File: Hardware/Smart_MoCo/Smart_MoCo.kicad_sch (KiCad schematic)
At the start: 57 parts, among them J1 Conn_02x02_Counter_Clockwise, Q1 BSS138, Q2 BSS138, Q3 BSS138, U1 VNH5019A-E, U2 STM32F042F6Px, U3 ATA6561, U4 AP62200WU, U5 AP62200WU

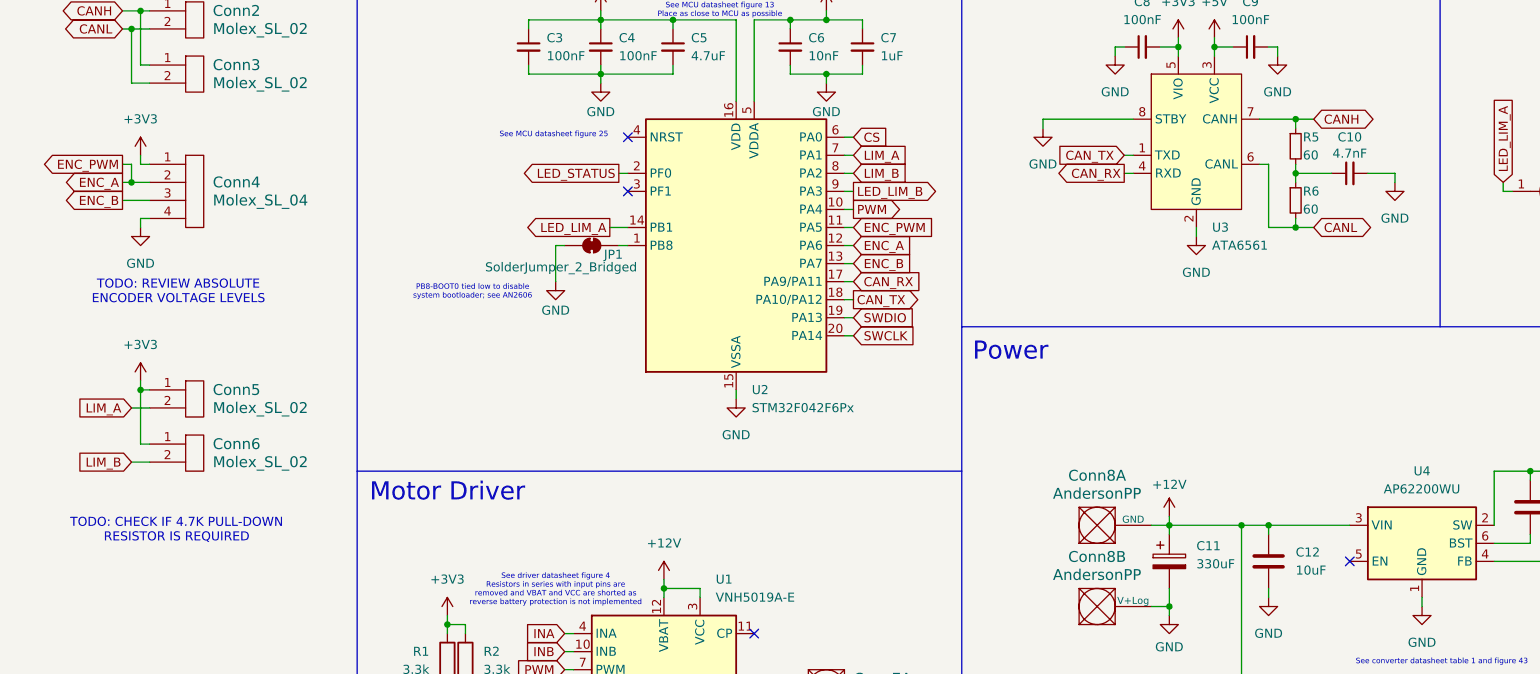
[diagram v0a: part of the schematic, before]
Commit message: Modify CAN circuit
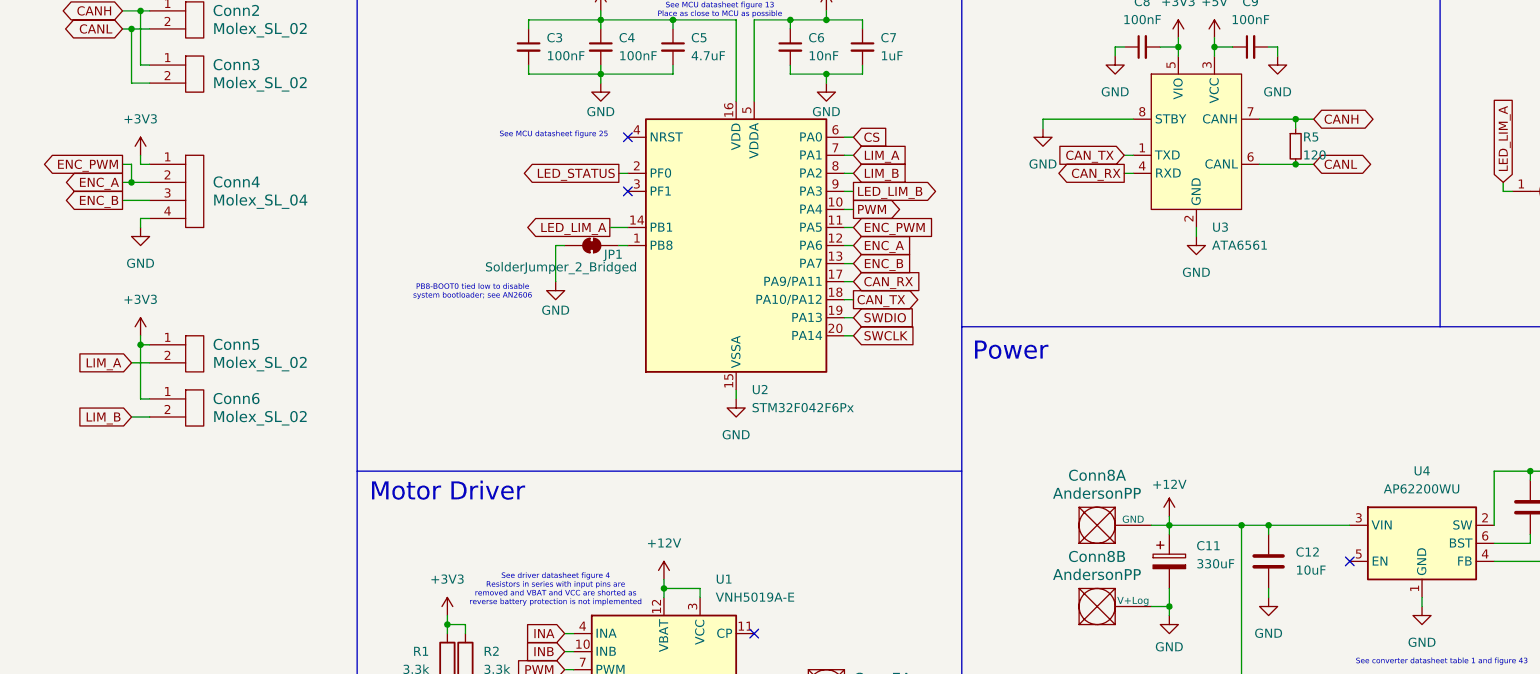
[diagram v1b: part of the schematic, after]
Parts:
- removed C10: 4.7nF, Capacitor_SMD:C_0603_1608Metric_Pad1.08x0.95mm_HandSolder, symbol Device:C_Small
- removed R6: 60, Resistor_SMD:R_0603_1608Metric_Pad0.98x0.95mm_HandSolder, symbol Device:R_Small
- R5: value 60 -> 120
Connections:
- net CANL: now also R5.2
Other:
- note removed: "TODO: CHECK IF 4.7K PULL-DOWN RESISTOR IS REQUIRED"
- note removed: "TODO: REVIEW ABSOLUTE ENCODER VOLTAGE LEVELS"
- moved on the sheet: Conn5, Conn6

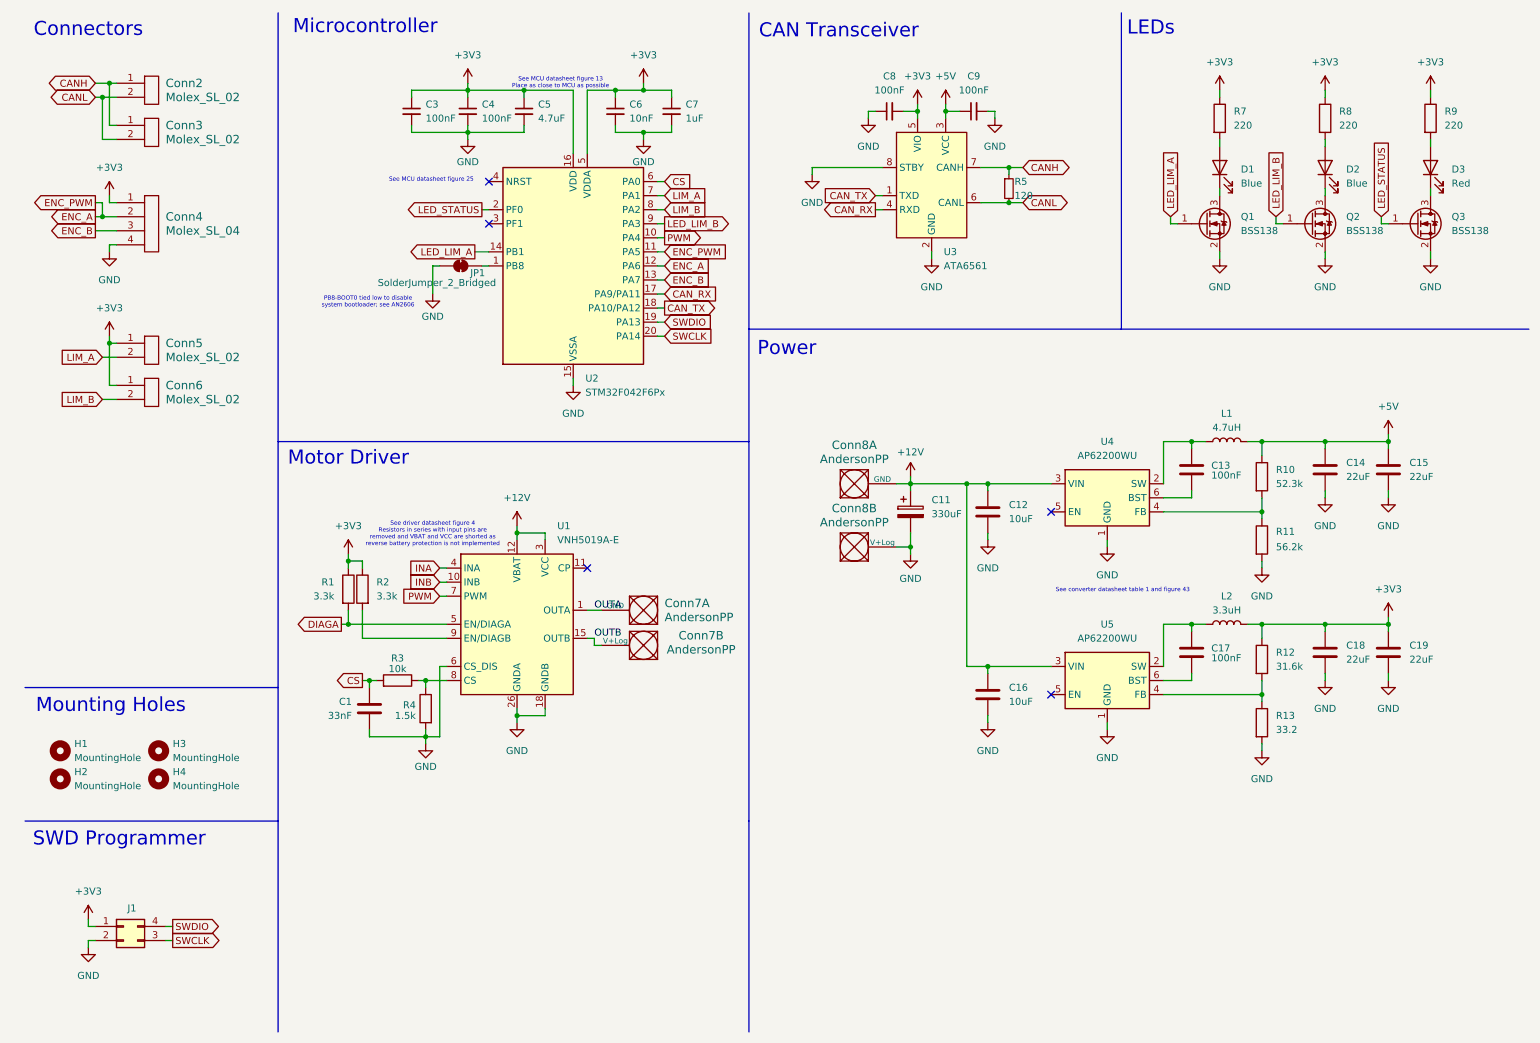
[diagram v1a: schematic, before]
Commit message: Implement schematic first review feedback and finish PCB layout
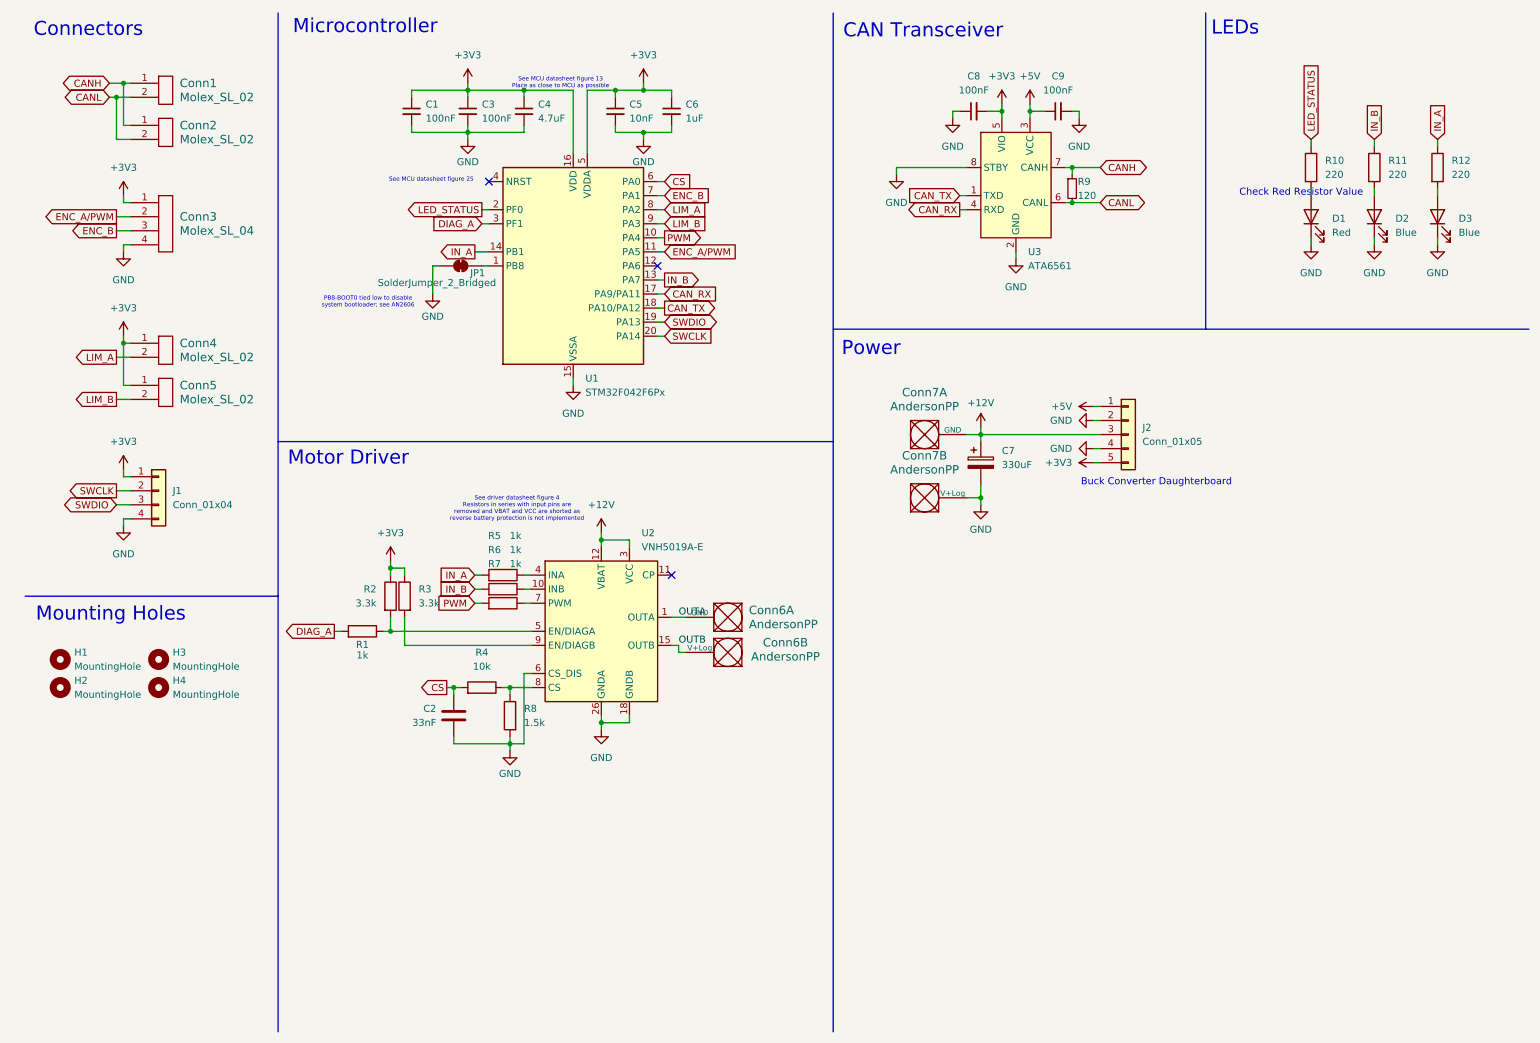
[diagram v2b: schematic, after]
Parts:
- removed C12, C16: 10uF, Capacitor_SMD:C_0603_1608Metric_Pad1.08x0.95mm_HandSolder, symbol Device:C
- removed C13, C17: 100nF, Capacitor_SMD:C_0603_1608Metric_Pad1.08x0.95mm_HandSolder, symbol Device:C
- removed C14, C15, C18, C19: 22uF, Capacitor_SMD:C_0603_1608Metric_Pad1.08x0.95mm_HandSolder, symbol Device:C
- removed J1: Conn_02x02_Counter_Clockwise, Connector_PinHeader_2.54mm:PinHeader_2x02_P2.54mm_Vertical, symbol Connector_Generic:Conn_02x02_Counter_Clockwise
- removed L1: 4.7uH, Inductor_SMD:L_1008_2520Metric_Pad1.43x2.20mm_HandSolder, symbol Device:L
- removed L2: 3.3uH, Inductor_SMD:L_1008_2520Metric_Pad1.43x2.20mm_HandSolder, symbol Device:L
- removed Q1, Q2, Q3: BSS138, Package_TO_SOT_SMD:SOT-23, symbol Transistor_FET:BSS138
- removed R12: 31.6k, Resistor_SMD:R_0603_1608Metric_Pad0.98x0.95mm_HandSolder, symbol Device:R
- removed R13: 33.2, Resistor_SMD:R_0603_1608Metric_Pad0.98x0.95mm_HandSolder, symbol Device:R
- removed R8: 220, Resistor_SMD:R_0603_1608Metric_Pad0.98x0.95mm_HandSolder, symbol Device:R
- removed U4, U5: AP62200WU, Package_TO_SOT_SMD:TSOT-23-6, symbol Regulator_Switching:AP62250WU
- added J1: Conn_01x04, Connector_PinSocket_2.54mm:PinSocket_1x04_P2.54mm_Vertical, symbol Connector_Generic:Conn_01x04
- added J2: Conn_01x05, Connector_PinSocket_2.54mm:PinSocket_1x05_P2.54mm_Vertical, symbol Connector_Generic:Conn_01x05
- added R1, R5, R6: 1k, Resistor_SMD:R_0603_1608Metric_Pad0.98x0.95mm_HandSolder, symbol Device:R
- Conn1: renamed from Conn2; footprint Library:MOLEX_SL_02_Horizontal_No_Holes -> MRDT_Connectors:MOLEX_SL_02_Vertical
- Conn2: renamed from Conn3; footprint Library:MOLEX_SL_02_Horizontal_No_Holes -> MRDT_Connectors:MOLEX_SL_02_Vertical
- Conn3: renamed from Conn4; footprint Library:MOLEX_SL_04_Horizontal_No_Holes -> MRDT_Connectors:MOLEX_SL_04_Vertical
- Conn4: renamed from Conn5; footprint Library:MOLEX_SL_02_Horizontal_No_Holes -> MRDT_Connectors:MOLEX_SL_02_Vertical
- Conn5: renamed from Conn6; footprint Library:MOLEX_SL_02_Horizontal_No_Holes -> MRDT_Connectors:MOLEX_SL_02_Vertical
- Conn6: renamed from Conn7; footprint MRDT_Connectors:Square_Anderson_2_H_Side_By_Side -> MRDT_Connectors:Square_Anderson_2_V_Side_By_Side
- Conn7: renamed from Conn8; footprint MRDT_Connectors:Square_Anderson_2_H_Side_By_Side -> MRDT_Connectors:Square_Anderson_2_V_Side_By_Side
- D1: value Blue -> Red
- D3: value Red -> Blue
- R10: value 52.3k -> 220
- R11: value 56.2k -> 220
- R7: value 220 -> 1k
- renumbered C3 to C1, C1 to C2, C4 to C3, C5 to C4, C6 to C5, C7 to C6, C11 to C7, R9 to R12, R1 to R2, R2 to R3, R3 to R4, R4 to R8, R5 to R9, U2 to U1, U1 to U2
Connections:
- net LED_LIM_B is gone; now on net LIM_B: U1.9 (PA3)
- net +12V: now also J2.3 (Pin_3)
- net +3V3: now also J1.1 (Pin_1), J2.5 (Pin_5); no longer R12.1, R7.1
- net +5V: now also J2.1 (Pin_1); no longer R10.1
- net ENC_B: now also U1.7 (PA1); no longer U1.13 (PA7)
- net GND: now also D1.1 (K), D2.1 (K), D3.1 (K), J1.4 (Pin_4), J2.2 (Pin_2), J2.4 (Pin_4); no longer R11.2
- net LED_STATUS: now also R10.1
- net LIM_A: now also U1.8 (PA2); no longer U1.7 (PA1)
- net LIM_B: no longer U1.8 (PA2)
- net PWM: now also R7.2; no longer U2.7 (PWM)
- net SWCLK: now also J1.2 (Pin_2)
- net SWDIO: now also J1.3 (Pin_3)
- net at D1.2 (A): now also R10.2; no longer R7.2
- net IN_B: now reaches R11.1
- net IN_B: now also U1.13 (PA7), R6.2; no longer R10.2
- net at D2.2 (A): now also R11.2
- net DIAG_A: now reaches U1.3 (PF1)
- net DIAG_A: now also R1.2
- net DIAGA: no longer names the net of R2.2, U2.5 (EN/DIAGA)
- net DIAGA: now also R1.1
- net ENC_A renamed ENC_A/PWM
- net ENC_A/PWM: no longer U1.12 (PA6)
- net INA: no longer names the net of U2.4 (INA)
- net INA: now also R5.1
- net INB: no longer names the net of U2.10 (INB)
- net INB: now also R6.1
- net LED_LIM_A renamed IN_A
- net IN_A: now also R12.1, R5.2
- new net: R7.1, U2.7 (PWM)
- no-connect marks 5 -> 3
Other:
- note added: "Buck Converter Daughterboard"
- note added: "Check Red Resistor Value"
- note removed: "SWD Programmer"
- note removed: "See converter datasheet table 1 and figure 43"
- moved on the sheet: C2, C7, C8, C9, Conn1, Conn2, Conn3, Conn4, Conn5, Conn6A, Conn6B, Conn7A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

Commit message: Prepare for board review
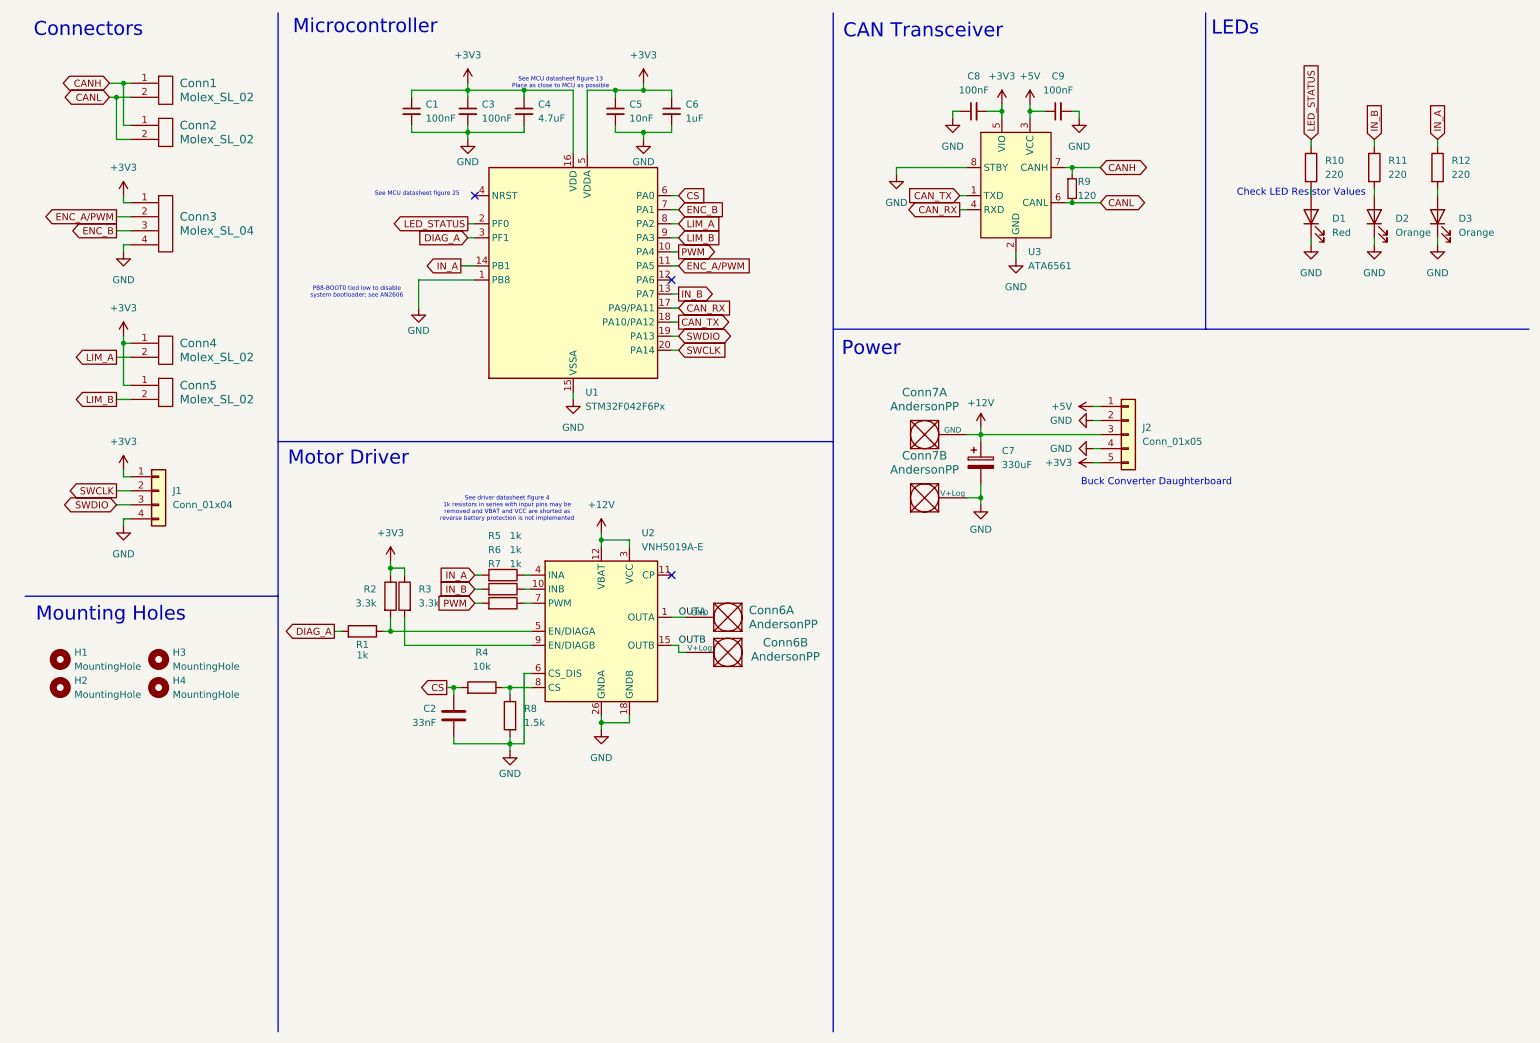
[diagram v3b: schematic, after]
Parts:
- removed JP1: SolderJumper_2_Bridged, Jumper:SolderJumper-2_P1.3mm_Bridged2Bar_RoundedPad1.0x1.5mm, symbol Jumper:SolderJumper_2_Bridged
- Conn6, Conn7: footprint MRDT_Connectors:Square_Anderson_2_V_Side_By_Side -> Local Libraries:Square_Anderson_2_V_Side_By_Side_No_Silkscreen
- D2, D3: value Blue -> Orange
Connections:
- net GND: now also U1.1 (PB8)
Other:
- note added: "Check LED Resistor Values"
- note added: "See driver datasheet figure 4 1k resistors in series with input pins may be removed and VBAT and VCC are shorted as reverse battery protection is not implemented"
- note removed: "Check Red Resistor Value"
- note removed: "See driver datasheet figure 4 Resistors in series with input pins are removed and VBAT and VCC are shorted as reverse battery protection is not implemented"
- company: (none) -> Mars Rover Design Team
- title: (none) -> Smart Brushed Motor Controller
- moved on the sheet: U1

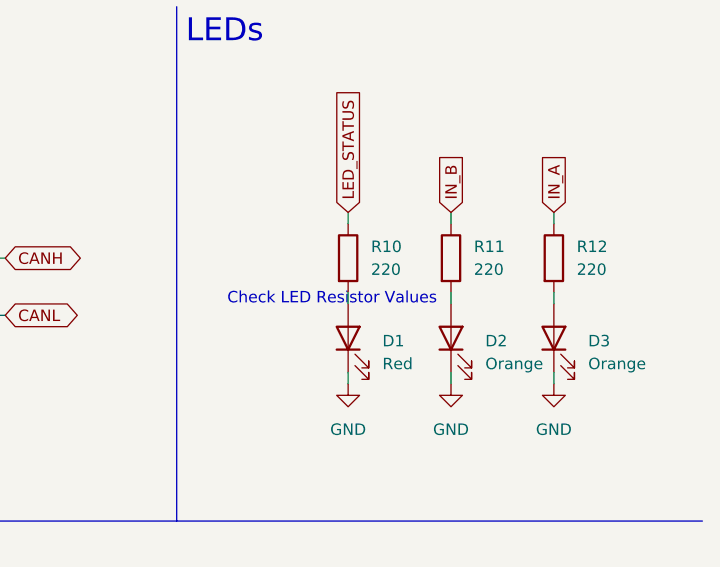
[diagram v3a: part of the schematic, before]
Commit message: Update LED resistor values
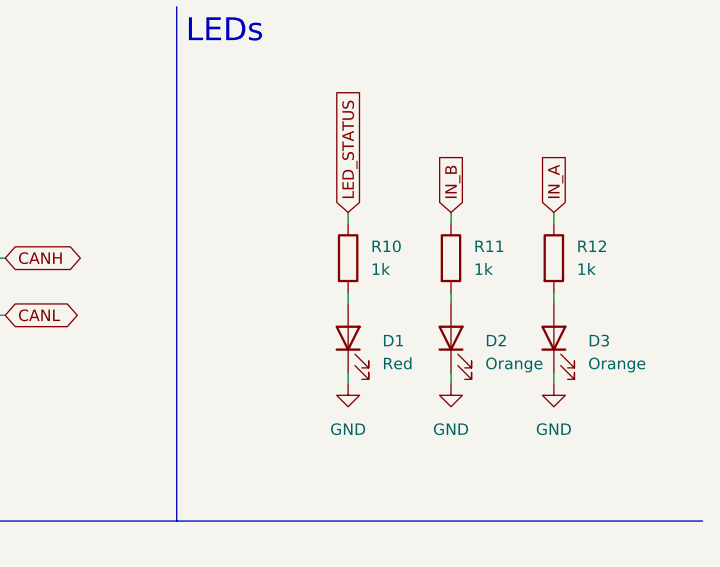
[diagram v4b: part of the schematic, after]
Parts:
- R10, R11, R12: value 220 -> 1k
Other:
- note removed: "Check LED Resistor Values"
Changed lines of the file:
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@@
 		)
 	)
-	(text "Check LED Resistor Values"
-		(exclude_from_sim no)
-		(at 243.332 45.212 0)
-		(effects
-			(font
-				(size 1.27 1.27)
-			)
-		)
-	)
 	(text "See MCU datasheet figure 25"
 		(exclude_from_sim no)
@@
 	(label "OUTA"
 		(at 130.81 121.92 0)
+		(fields_autoplaced yes)
 		(effects
 			(font
@@
 	(label "OUTB"
 		(at 130.81 127 0)
+		(fields_autoplaced yes)
 		(effects
 			(font
@@
 			)
 		)
-		(property "Value" "220"
+		(property "Value" "1k"
 			(at 247.65 41.9099 0)
 			(effects
@@
 			)
 		)
-		(property "Value" "220"
+		(property "Value" "1k"
 			(at 270.51 41.9099 0)
 			(effects
@@
 			)
 		)
-		(property "Value" "220"
+		(property "Value" "1k"
 			(at 259.08 41.9099 0)
 			(effects
